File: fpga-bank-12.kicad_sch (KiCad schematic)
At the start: 1 part, among them U4 XC7K160T-FFG676

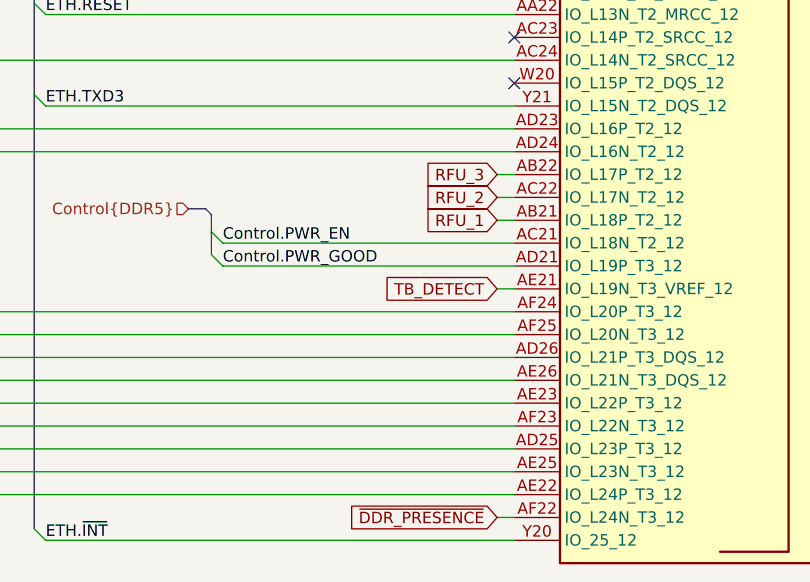
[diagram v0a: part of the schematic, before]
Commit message: Changing SO-DIMM sch to UDIMM
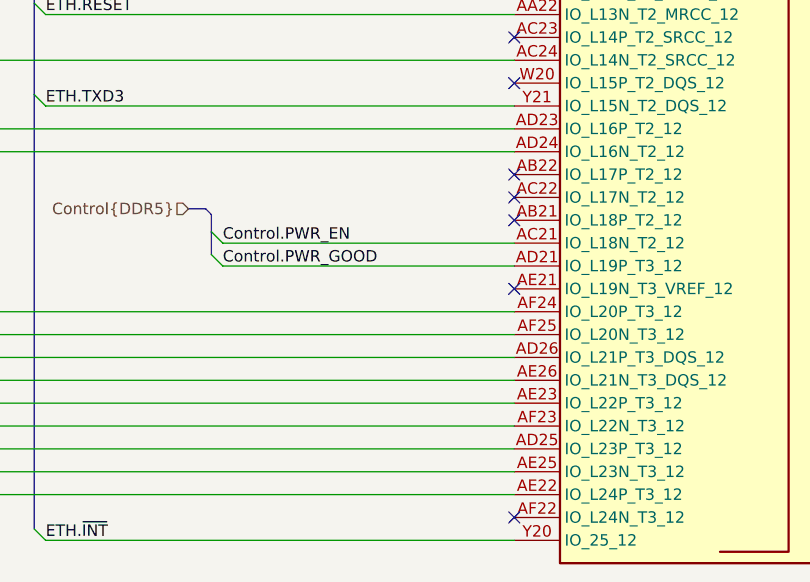
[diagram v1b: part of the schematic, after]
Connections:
- net RFU_1: no longer names the net of U4.AB21 (IO_L18P_T2_12)
- net RFU_2: no longer names the net of U4.AC22 (IO_L17N_T2_12)
- net RFU_3: no longer names the net of U4.AB22 (IO_L17P_T2_12)
- net TB_DETECT: no longer names the net of U4.AE21 (IO_L19N_T3_VREF_12)
- net ~{DDR_PRESENCE}: no longer names the net of U4.AF22 (IO_L24N_T3_12)
- no-connect marks 13 -> 18
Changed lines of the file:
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@@
   (no_connect (at 191.77 124.46))
   (no_connect (at 191.77 104.14))
+  (no_connect (at 191.77 175.26))
+  (no_connect (at 191.77 185.42))
+  (no_connect (at 191.77 210.82))
+  (no_connect (at 191.77 172.72))
   (no_connect (at 191.77 162.56))
   (no_connect (at 191.77 144.78))
@@
   (no_connect (at 191.77 157.48))
   (no_connect (at 191.77 119.38))
+  (no_connect (at 191.77 177.8))
   (no_connect (at 191.77 127))
   (no_connect (at 191.77 91.44))
@@
     (stroke (width 0) (type default))
   )
-  (wire (pts (xy 189.865 172.72) (xy 191.77 172.72))
-    (stroke (width 0) (type default))
-  )
   (wire (pts (xy 139.7 129.54) (xy 191.77 129.54))
     (stroke (width 0) (type default))
@@
     (stroke (width 0) (type default))
   )
-  (wire (pts (xy 189.865 185.42) (xy 191.77 185.42))
-    (stroke (width 0) (type default))
-  )
   (bus (pts (xy 138.43 151.13) (xy 138.43 153.67))
     (stroke (width 0) (type default))
@@
     (stroke (width 0) (type default))
   )
-  (wire (pts (xy 189.865 177.8) (xy 191.77 177.8))
-    (stroke (width 0) (type default))
-  )
   (wire (pts (xy 139.7 139.7) (xy 191.77 139.7))
     (stroke (width 0) (type default))
@@
     (stroke (width 0) (type default))
   )
-  (wire (pts (xy 189.865 175.26) (xy 191.77 175.26))
-    (stroke (width 0) (type default))
-  )
   (wire (pts (xy 117.475 170.18) (xy 191.77 170.18))
     (stroke (width 0) (type default))
@@
   )
   (wire (pts (xy 139.7 109.22) (xy 191.77 109.22))
-    (stroke (width 0) (type default))
-  )
-  (wire (pts (xy 189.865 210.82) (xy 191.77 210.82))
     (stroke (width 0) (type default))
   )
@@
     (effects (font (size 1.27 1.27)) (justify left bottom))
   )
-  (global_label "RFU_1" (shape input) (at 189.865 177.8 180) (fields_autoplaced)
-    (effects (font (size 1.27 1.27)) (justify right))
-    (property "Intersheetrefs" "${INTERSHEET_REFS}" (at 181.6746 177.7206 0)
-      (effects (font (size 1.27 1.27)) (justify right))
-    )
-  )
-  (global_label "RFU_3" (shape input) (at 189.865 172.72 180) (fields_autoplaced)
-    (effects (font (size 1.27 1.27)) (justify right))
-    (property "Intersheetrefs" "${INTERSHEET_REFS}" (at 181.6746 172.6406 0)
-      (effects (font (size 1.27 1.27)) (justify right))
-    )
-  )
-  (global_label "RFU_2" (shape input) (at 189.865 175.26 180) (fields_autoplaced)
-    (effects (font (size 1.27 1.27)) (justify right))
-    (property "Intersheetrefs" "${INTERSHEET_REFS}" (at 181.6746 175.3394 0)
-      (effects (font (size 1.27 1.27)) (justify right))
-    )
-  )
-  (global_label "TB_DETECT" (shape input) (at 189.865 185.42 180) (fields_autoplaced)
-    (effects (font (size 1.27 1.27)) (justify right))
-    (property "Intersheetrefs" "${INTERSHEET_REFS}" (at 177.5622 185.4994 0)
-      (effects (font (size 1.27 1.27)) (justify right))
-    )
-  )
-  (global_label "~{DDR_PRESENCE}" (shape input) (at 189.865 210.82 180) (fields_autoplaced)
-    (effects (font (size 1.27 1.27)) (justify right))
-    (property "Intersheetrefs" "${INTERSHEET_REFS}" (at 172.966 210.8994 0)
-      (effects (font (size 1.27 1.27)) (justify right))
-    )
-  )
   (hierarchical_label "Control{DDR5}" (shape input) (at 155.575 176.53 180) (fields_autoplaced)
